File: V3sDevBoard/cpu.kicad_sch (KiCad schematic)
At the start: 1 part, among them U1 Allwinner_V3s

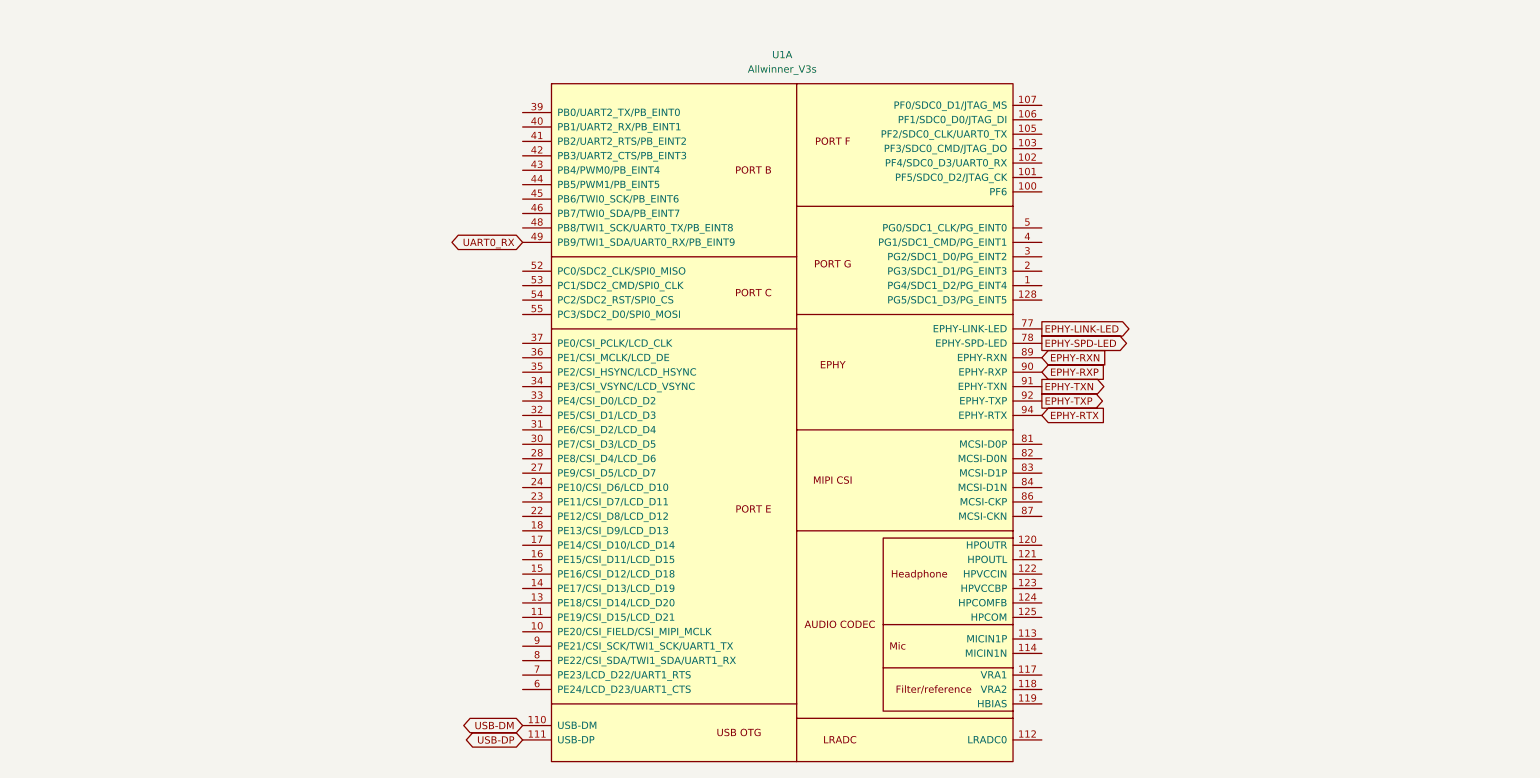
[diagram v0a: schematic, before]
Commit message: drawing schematic
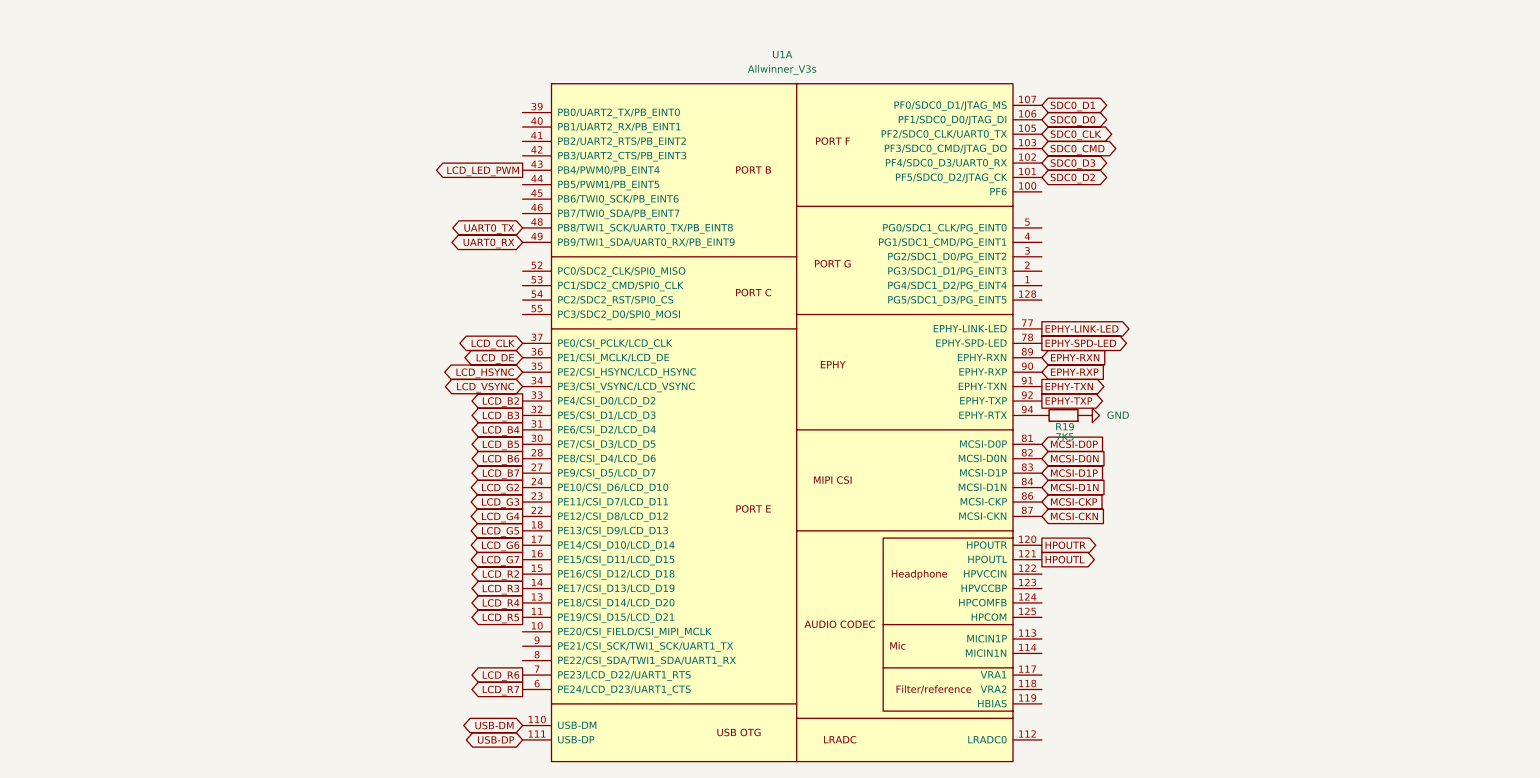
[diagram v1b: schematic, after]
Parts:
- added R19: 7K5, symbol Device:R
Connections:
- net SDC0_D2: now reaches U1.101 (PF5/SDC0_D2/JTAG_CK)
- net SDC0_D3: now reaches U1.102 (PF4/SDC0_D3/UART0_RX)
- net SDC0_CMD: now reaches U1.103 (PF3/SDC0_CMD/JTAG_DO)
- net SDC0_CLK: now reaches U1.105 (PF2/SDC0_CLK/UART0_TX)
- net SDC0_D0: now reaches U1.106 (PF1/SDC0_D0/JTAG_DI)
- net SDC0_D1: now reaches U1.107 (PF0/SDC0_D1/JTAG_MS)
- net LCD_R5: now reaches U1.11 (PE19/CSI_D15/LCD_D21)
- net HPOUTR: now reaches U1.120 (HPOUTR)
- net HPOUTL: now reaches U1.121 (HPOUTL)
- net LCD_R4: now reaches U1.13 (PE18/CSI_D14/LCD_D20)
- net LCD_R3: now reaches U1.14 (PE17/CSI_D13/LCD_D19)
- net LCD_R2: now reaches U1.15 (PE16/CSI_D12/LCD_D18)
- net LCD_G7: now reaches U1.16 (PE15/CSI_D11/LCD_D15)
- net LCD_G6: now reaches U1.17 (PE14/CSI_D10/LCD_D14)
- net LCD_G5: now reaches U1.18 (PE13/CSI_D9/LCD_D13)
- net LCD_G4: now reaches U1.22 (PE12/CSI_D8/LCD_D12)
- net LCD_G3: now reaches U1.23 (PE11/CSI_D7/LCD_D11)
- net LCD_G2: now reaches U1.24 (PE10/CSI_D6/LCD_D10)
- net LCD_B7: now reaches U1.27 (PE9/CSI_D5/LCD_D7)
- net LCD_B6: now reaches U1.28 (PE8/CSI_D4/LCD_D6)
- net LCD_B5: now reaches U1.30 (PE7/CSI_D3/LCD_D5)
- net LCD_B4: now reaches U1.31 (PE6/CSI_D2/LCD_D4)
- net LCD_B3: now reaches U1.32 (PE5/CSI_D1/LCD_D3)
- net LCD_B2: now reaches U1.33 (PE4/CSI_D0/LCD_D2)
- net LCD_VSYNC: now reaches U1.34 (PE3/CSI_VSYNC/LCD_VSYNC)
- net LCD_HSYNC: now reaches U1.35 (PE2/CSI_HSYNC/LCD_HSYNC)
- net LCD_DE: now reaches U1.36 (PE1/CSI_MCLK/LCD_DE)
- net LCD_CLK: now reaches U1.37 (PE0/CSI_PCLK/LCD_CLK)
- net LCD_LED_PWM: now reaches U1.43 (PB4/PWM0/PB_EINT4)
- net UART0_TX: now reaches U1.48 (PB8/TWI1_SCK/UART0_TX/PB_EINT8)
- net LCD_R7: now reaches U1.6 (PE24/LCD_D23/UART1_CTS)
- net LCD_R6: now reaches U1.7 (PE23/LCD_D22/UART1_RTS)
- net MCSI-D0P: now reaches U1.81 (MCSI-D0P)
- net MCSI-D0N: now reaches U1.82 (MCSI-D0N)
- net MCSI-D1P: now reaches U1.83 (MCSI-D1P)
- net MCSI-D1N: now reaches U1.84 (MCSI-D1N)
- net MCSI-CKP: now reaches U1.86 (MCSI-CKP)
- net MCSI-CKN: now reaches U1.87 (MCSI-CKN)
- net EPHY-RTX: no longer names the net of U1.94 (EPHY-RTX)
- net EPHY-RTX: now also R19.1
- new net GND: R19.2

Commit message: drawing schematics
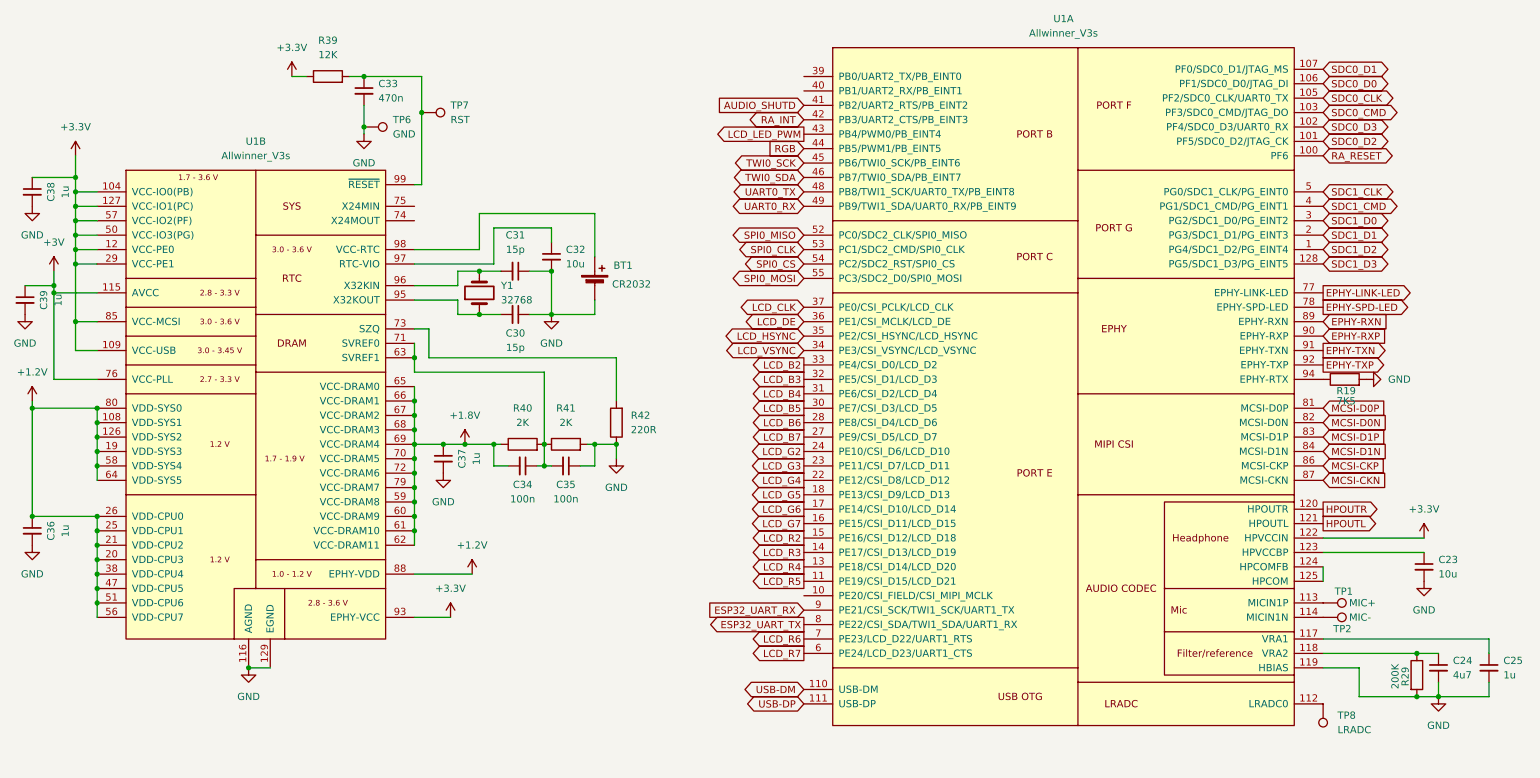
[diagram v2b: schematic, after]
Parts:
- added BT1: CR2032, Battery:BatteryHolder_MYOUNG_BS-07-A1BJ001_CR2032, symbol Device:Battery_Cell
- added C23, C32: 10u, Capacitor_SMD:C_0805_2012Metric_Pad1.18x1.45mm_HandSolder, symbol Device:C_Small
- added C24: 4u7, Capacitor_SMD:C_0805_2012Metric_Pad1.18x1.45mm_HandSolder, symbol Device:C_Small
- added C25, C36, C37, C38, C39: 1u, Capacitor_SMD:C_0805_2012Metric_Pad1.18x1.45mm_HandSolder, symbol Device:C_Small
- added C30, C31: 15p, Capacitor_SMD:C_0805_2012Metric_Pad1.18x1.45mm_HandSolder, symbol Device:C_Small
- added C33: 470n, Capacitor_SMD:C_0805_2012Metric_Pad1.18x1.45mm_HandSolder, symbol Device:C_Small
- added C34, C35: 100n, Capacitor_SMD:C_0805_2012Metric_Pad1.18x1.45mm_HandSolder, symbol Device:C_Small
- added R29: 200K, Resistor_SMD:R_0805_2012Metric_Pad1.20x1.40mm_HandSolder, symbol Device:R
- added R39: 12K, Resistor_SMD:R_0805_2012Metric_Pad1.20x1.40mm_HandSolder, symbol Device:R
- added R40, R41: 2K, Resistor_SMD:R_0805_2012Metric_Pad1.20x1.40mm_HandSolder, symbol Device:R
- added R42: 220R, Resistor_SMD:R_0805_2012Metric_Pad1.20x1.40mm_HandSolder, symbol Device:R
- added TP1: MIC+, TestPoint:TestPoint_Pad_D1.0mm, symbol Connector:TestPoint
- added TP2: MIC-, TestPoint:TestPoint_Pad_D1.0mm, symbol Connector:TestPoint
- added TP6: GND, TestPoint:TestPoint_Pad_D1.5mm, symbol Connector:TestPoint
- added TP7: RST, TestPoint:TestPoint_Pad_D1.5mm, symbol Connector:TestPoint
- added TP8: LRADC, TestPoint:TestPoint_Pad_D1.0mm, symbol Connector:TestPoint
- added unit 1 of U1
- added Y1: 32768, Crystal:Crystal_SMD_Abracon_ABS25-4Pin_8.0x3.8mm, symbol Device:Crystal
- R19: footprint (none) -> Resistor_SMD:R_0805_2012Metric_Pad1.20x1.40mm_HandSolder
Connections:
- net EPHY-LINK-LED: now also U1.77 (EPHY-LINK-LED); no longer U1.77 (EPHY-LINK-LED)
- net EPHY-RXN: now also U1.89 (EPHY-RXN); no longer U1.89 (EPHY-RXN)
- net EPHY-RXP: now also U1.90 (EPHY-RXP); no longer U1.90 (EPHY-RXP)
- net EPHY-SPD-LED: now also U1.78 (EPHY-SPD-LED); no longer U1.78 (EPHY-SPD-LED)
- net EPHY-TXN: now also U1.91 (EPHY-TXN); no longer U1.91 (EPHY-TXN)
- net EPHY-TXP: now also U1.92 (EPHY-TXP); no longer U1.92 (EPHY-TXP)
- net GND: now also U1.116 (AGND), U1.129 (EGND), BT1.2 (-), C23.2, C24.2, C25.2, C30.1, C31.1, C32.2, C33.2, C35.1, C36.2, C37.2, C38.2, C39.2, R29.2, R41.2, R42.1, TP6.1, U1.119 (HBIAS)
- net HPOUTL: now also U1.121 (HPOUTL); no longer U1.121 (HPOUTL)
- net HPOUTR: now also U1.120 (HPOUTR); no longer U1.120 (HPOUTR)
- net LCD_B2: now also U1.33 (PE4/CSI_D0/LCD_D2); no longer U1.33 (PE4/CSI_D0/LCD_D2)
- net LCD_B3: now also U1.32 (PE5/CSI_D1/LCD_D3); no longer U1.32 (PE5/CSI_D1/LCD_D3)
- net LCD_B4: now also U1.31 (PE6/CSI_D2/LCD_D4); no longer U1.31 (PE6/CSI_D2/LCD_D4)
- net LCD_B5: now also U1.30 (PE7/CSI_D3/LCD_D5); no longer U1.30 (PE7/CSI_D3/LCD_D5)
- net LCD_B6: now also U1.28 (PE8/CSI_D4/LCD_D6); no longer U1.28 (PE8/CSI_D4/LCD_D6)
- net LCD_B7: now also U1.27 (PE9/CSI_D5/LCD_D7); no longer U1.27 (PE9/CSI_D5/LCD_D7)
- net LCD_CLK: now also U1.37 (PE0/CSI_PCLK/LCD_CLK); no longer U1.37 (PE0/CSI_PCLK/LCD_CLK)
- net LCD_DE: now also U1.36 (PE1/CSI_MCLK/LCD_DE); no longer U1.36 (PE1/CSI_MCLK/LCD_DE)
- net LCD_G2: now also U1.24 (PE10/CSI_D6/LCD_D10); no longer U1.24 (PE10/CSI_D6/LCD_D10)
- net LCD_G3: now also U1.23 (PE11/CSI_D7/LCD_D11); no longer U1.23 (PE11/CSI_D7/LCD_D11)
- net LCD_G4: now also U1.22 (PE12/CSI_D8/LCD_D12); no longer U1.22 (PE12/CSI_D8/LCD_D12)
- net LCD_G5: now also U1.18 (PE13/CSI_D9/LCD_D13); no longer U1.18 (PE13/CSI_D9/LCD_D13)
- net LCD_G6: now also U1.17 (PE14/CSI_D10/LCD_D14); no longer U1.17 (PE14/CSI_D10/LCD_D14)
- net LCD_G7: now also U1.16 (PE15/CSI_D11/LCD_D15); no longer U1.16 (PE15/CSI_D11/LCD_D15)
- net LCD_HSYNC: now also U1.35 (PE2/CSI_HSYNC/LCD_HSYNC); no longer U1.35 (PE2/CSI_HSYNC/LCD_HSYNC)
- net LCD_LED_PWM: now also U1.43 (PB4/PWM0/PB_EINT4); no longer U1.43 (PB4/PWM0/PB_EINT4)
- net LCD_R2: now also U1.15 (PE16/CSI_D12/LCD_D18); no longer U1.15 (PE16/CSI_D12/LCD_D18)
- net LCD_R3: now also U1.14 (PE17/CSI_D13/LCD_D19); no longer U1.14 (PE17/CSI_D13/LCD_D19)
- net LCD_R4: now also U1.13 (PE18/CSI_D14/LCD_D20); no longer U1.13 (PE18/CSI_D14/LCD_D20)
- net LCD_R5: now also U1.11 (PE19/CSI_D15/LCD_D21); no longer U1.11 (PE19/CSI_D15/LCD_D21)
- net LCD_R6: now also U1.7 (PE23/LCD_D22/UART1_RTS); no longer U1.7 (PE23/LCD_D22/UART1_RTS)
- net LCD_R7: now also U1.6 (PE24/LCD_D23/UART1_CTS); no longer U1.6 (PE24/LCD_D23/UART1_CTS)
- net LCD_VSYNC: now also U1.34 (PE3/CSI_VSYNC/LCD_VSYNC); no longer U1.34 (PE3/CSI_VSYNC/LCD_VSYNC)
- net MCSI-CKN: now also U1.87 (MCSI-CKN); no longer U1.87 (MCSI-CKN)
- net MCSI-CKP: now also U1.86 (MCSI-CKP); no longer U1.86 (MCSI-CKP)
- net MCSI-D0N: now also U1.82 (MCSI-D0N); no longer U1.82 (MCSI-D0N)
- net MCSI-D0P: now also U1.81 (MCSI-D0P); no longer U1.81 (MCSI-D0P)
- net MCSI-D1N: now also U1.84 (MCSI-D1N); no longer U1.84 (MCSI-D1N)
- net MCSI-D1P: now also U1.83 (MCSI-D1P); no longer U1.83 (MCSI-D1P)
- net SDC0_CLK: now also U1.105 (PF2/SDC0_CLK/UART0_TX); no longer U1.105 (PF2/SDC0_CLK/UART0_TX)
- net SDC0_CMD: now also U1.103 (PF3/SDC0_CMD/JTAG_DO); no longer U1.103 (PF3/SDC0_CMD/JTAG_DO)
- net SDC0_D0: now also U1.106 (PF1/SDC0_D0/JTAG_DI); no longer U1.106 (PF1/SDC0_D0/JTAG_DI)
- net SDC0_D1: now also U1.107 (PF0/SDC0_D1/JTAG_MS); no longer U1.107 (PF0/SDC0_D1/JTAG_MS)
- net SDC0_D2: now also U1.101 (PF5/SDC0_D2/JTAG_CK); no longer U1.101 (PF5/SDC0_D2/JTAG_CK)
- net SDC0_D3: now also U1.102 (PF4/SDC0_D3/UART0_RX); no longer U1.102 (PF4/SDC0_D3/UART0_RX)
- net UART0_RX: now also U1.49 (PB9/TWI1_SDA/UART0_RX/PB_EINT9); no longer U1.49 (PB9/TWI1_SDA/UART0_RX/PB_EINT9)
- net UART0_TX: now also U1.48 (PB8/TWI1_SCK/UART0_TX/PB_EINT8); no longer U1.48 (PB8/TWI1_SCK/UART0_TX/PB_EINT8)
- net USB-DM: now also U1.110 (USB-DM); no longer U1.110 (USB-DM)
- net USB-DP: now also U1.111 (USB-DP); no longer U1.111 (USB-DP)
- net at R19.1: now also U1.94 (EPHY-RTX); no longer U1.94 (EPHY-RTX)
- new net: TP1.1, U1.113 (MICIN1P)
- new net: TP2.1, U1.114 (MICIN1N)
- new net: C34.1, C35.2, R40.2, R41.1, U1.63 (SVREF1), U1.71 (SVREF0)
- new net: R42.2, U1.73 (SZQ)
- new net: C30.2, U1.95 (X32KOUT), Y1.1
- new net: C31.2, U1.96 (X32KIN), Y1.4 (2)
- new net: C32.1, U1.97 (RTC-VIO)
- new net: BT1.1 (+), U1.98 (VCC-RTC)
- new net: C33.1, R39.2, TP7.1, U1.99 (~{RESET})
- new net: TP8.1, U1.112 (LRADC0)
- new net: C25.1, U1.117 (VRA1)
- new net: C24.1, R29.1, U1.118 (VRA2)
- new net: C23.1, U1.123 (HPVCCBP)
- new net: U1.124 (HPCOMFB), U1.125 (HPCOM)
- new net +1.2V: C36.1, U1.108 (VDD-SYS1), U1.126 (VDD-SYS2), U1.19 (VDD-SYS3), U1.20 (VDD-CPU3), U1.21 (VDD-CPU2), U1.25 (VDD-CPU1), U1.26 (VDD-CPU0), U1.38 (VDD-CPU4), U1.47 (VDD-CPU5), U1.51 (VDD-CPU6), U1.56 (VDD-CPU7), U1.58 (VDD-SYS4), U1.64 (VDD-SYS5), U1.80 (VDD-SYS0), U1.88 (EPHY-VDD)
- new net +1.8V: C34.2, C37.1, R40.1, U1.59 (VCC-DRAM8), U1.60 (VCC-DRAM9), U1.61 (VCC-DRAM10), U1.62 (VCC-DRAM11), U1.65 (VCC-DRAM0), U1.66 (VCC-DRAM1), U1.67 (VCC-DRAM2), U1.68 (VCC-DRAM3), U1.69 (VCC-DRAM4), U1.70 (VCC-DRAM5), U1.72 (VCC-DRAM6), U1.79 (VCC-DRAM7)
- new net +3.3V: C38.1, R39.1, U1.104 (VCC-IO0(PB)), U1.109 (VCC-USB), U1.12 (VCC-PE0), U1.122 (HPVCCIN), U1.127 (VCC-IO1(PC)), U1.29 (VCC-PE1), U1.50 (VCC-IO3(PG)), U1.57 (VCC-IO2(PF)), U1.85 (VCC-MCSI), U1.93 (EPHY-VCC)
- new net +3V: C39.1, U1.115 (AVCC), U1.76 (VCC-PLL)
- new net AUDIO_SHUTD: U1.41 (PB2/UART2_RTS/PB_EINT2)
- new net ESP32_UART_RX: U1.9 (PE21/CSI_SCK/TWI1_SCK/UART1_TX)
- new net ESP32_UART_TX: U1.8 (PE22/CSI_SDA/TWI1_SDA/UART1_RX)
- new net RA_INT: U1.42 (PB3/UART2_CTS/PB_EINT3)
- new net RA_RESET: U1.100 (PF6)
- new net RGB: U1.44 (PB5/PWM1/PB_EINT5)
- new net SDC1_CLK: U1.5 (PG0/SDC1_CLK/PG_EINT0)
- new net SDC1_CMD: U1.4 (PG1/SDC1_CMD/PG_EINT1)
- new net SDC1_D0: U1.3 (PG2/SDC1_D0/PG_EINT2)
- new net SDC1_D1: U1.2 (PG3/SDC1_D1/PG_EINT3)
- new net SDC1_D2: U1.1 (PG4/SDC1_D2/PG_EINT4)
- new net SDC1_D3: U1.128 (PG5/SDC1_D3/PG_EINT5)
- new net SPI0_CLK: U1.53 (PC1/SDC2_CMD/SPI0_CLK)
- new net SPI0_CS: U1.54 (PC2/SDC2_RST/SPI0_CS)
- new net SPI0_MISO: U1.52 (PC0/SDC2_CLK/SPI0_MISO)
- new net SPI0_MOSI: U1.55 (PC3/SDC2_D0/SPI0_MOSI)
- new net TWI0_SCK: U1.45 (PB6/TWI0_SCK/PB_EINT6)
- new net TWI0_SDA: U1.46 (PB7/TWI0_SDA/PB_EINT7)
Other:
- company: (none) -> J.K.
- title: (none) -> V3s Dev Board
- moved on the sheet: R19

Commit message: advancing in schematics and footprints
Making needed custom footprints for connectors, adding a lot of small changes to schematics.
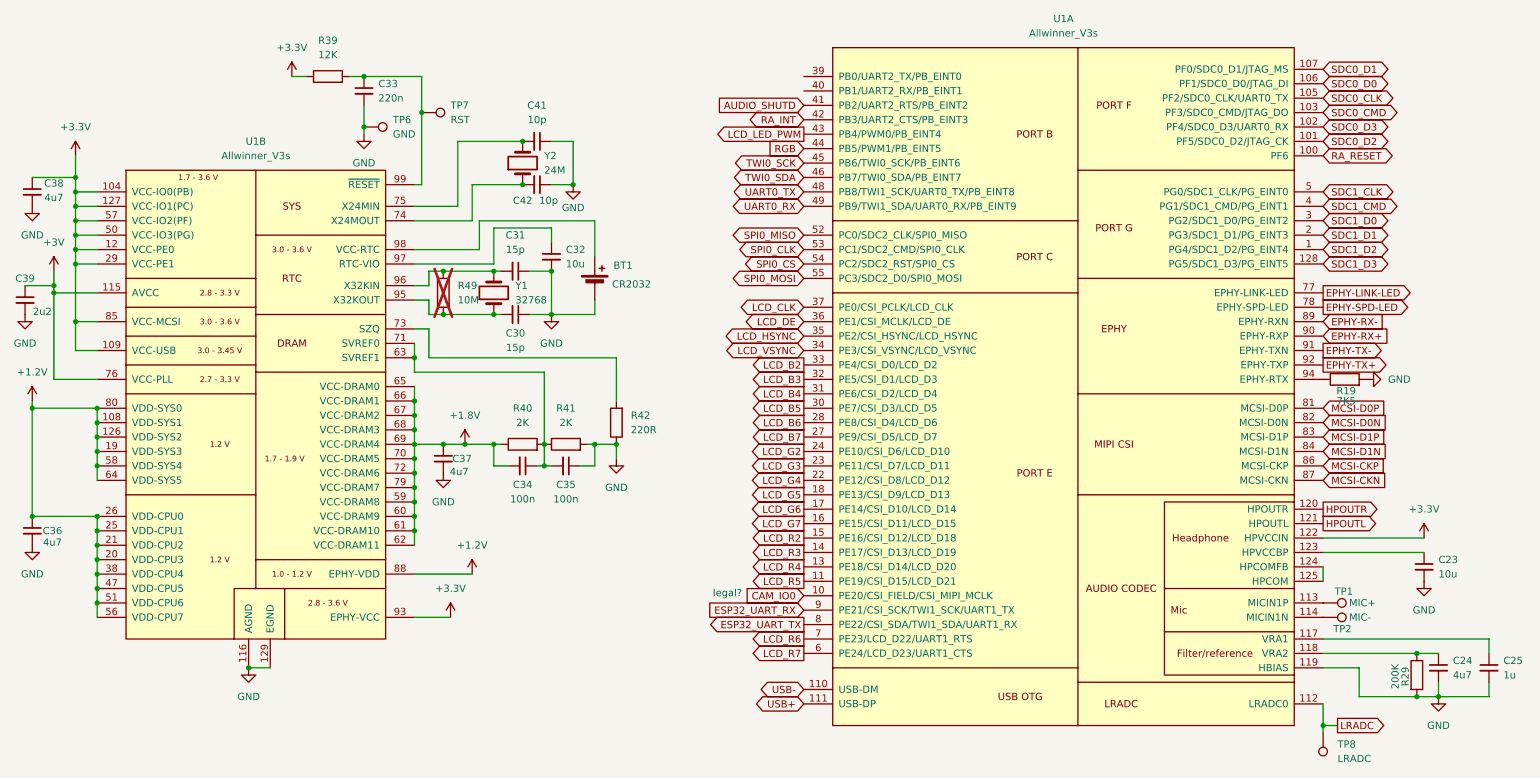
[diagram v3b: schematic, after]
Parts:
- added C41, C42: 10p, Capacitor_SMD:C_0805_2012Metric_Pad1.18x1.45mm_HandSolder, symbol Device:C_Small
- added R49: 10M, Resistor_SMD:R_0805_2012Metric_Pad1.20x1.40mm_HandSolder, symbol Device:R
- added Y2: 24M, Crystal:Crystal_HC49-4H_Vertical, symbol Device:Crystal
- C33: value 470n -> 220n
- C36, C37, C38: value 1u -> 4u7
- C39: value 1u -> 2u2
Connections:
- net GND: now also C41.1, C42.1
- net at U1.74 (X24MOUT): now also C42.2, Y2.1
- net at U1.75 (X24MIN): now also C41.2, Y2.4 (2)
- net at C30.2, U1.95 (X32KOUT), Y1.1: now also R49.1
- net at C31.2, U1.96 (X32KIN), Y1.4 (2): now also R49.2
- net CAM_IO0: now reaches U1.10 (PE20/CSI_FIELD/CSI_MIPI_MCLK)
- net LRADC: now reaches TP8.1, U1.112 (LRADC0)
- net EPHY-RXN renamed EPHY-RX-
- net EPHY-RXP renamed EPHY-RX+
- net EPHY-TXN renamed EPHY-TX-
- net EPHY-TXP renamed EPHY-TX+
- net USB-DM renamed USB-
- net USB-DP renamed USB+
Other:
- note added: "legal?"
- title: V3s Dev Board -> V3s_Dev_Board
- moved on the sheet: TP8, Y1

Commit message: completing schematics
completing schematics, adding netclasses, fixing bugs, updating readme, starting pcb
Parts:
- added R63, R64, R65, R66: 33R, Resistor_SMD:R_0603_1608Metric_Pad0.98x0.95mm_HandSolder, symbol Device:R
- added R67: 470R, Resistor_SMD:R_0603_1608Metric_Pad0.98x0.95mm_HandSolder, symbol Device:R
- added TP18: CAM_IO0, TestPoint:TestPoint_Pad_D1.0mm, symbol Connector:TestPoint
- added TP19: PF6, TestPoint:TestPoint_Pad_D1.0mm, symbol Connector:TestPoint
- C32: value 10u -> 4u7
- R19: value 7K5 -> 5K6; footprint Resistor_SMD:R_0805_2012Metric_Pad1.20x1.40mm_HandSolder -> Resistor_SMD:R_0603_1608Metric_Pad0.98x0.95mm_HandSolder
- R42: value 220R -> 240R 1%
- TP1, TP2: footprint TestPoint:TestPoint_Pad_D1.0mm -> TestPoint:TestPoint_Pad_1.0x1.0mm
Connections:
- net AUDIO_SHUTD is gone; now on net RA_RESET: U1.41 (PB2/UART2_RTS/PB_EINT2)
- net CAM_IO0: now also TP18.1
- net ESP32_UART_RX: now also U1.39 (PB0/UART2_TX/PB_EINT0); no longer U1.9 (PE21/CSI_SCK/TWI1_SCK/UART1_TX)
- net ESP32_UART_TX: now also U1.40 (PB1/UART2_RX/PB_EINT1); no longer U1.8 (PE22/CSI_SDA/TWI1_SDA/UART1_RX)
- net GND: now also R67.2; no longer R19.2
- net LCD_CLK: now also R64.1; no longer U1.37 (PE0/CSI_PCLK/LCD_CLK)
- net RA_RESET: no longer U1.100 (PF6)
- net SDC0_CLK: now also R63.2; no longer U1.105 (PF2/SDC0_CLK/UART0_TX)
- net SDC1_CLK: now also R66.2; no longer U1.5 (PG0/SDC1_CLK/PG_EINT0)
- net SPI0_CLK: now also R65.1; no longer U1.53 (PC1/SDC2_CMD/SPI0_CLK)
- net at C41.2, U1.75 (X24MIN): now also Y2.2; no longer Y2.4 (2)
- net HPCOM: now reaches U1.124 (HPCOMFB), U1.125 (HPCOM)
- new net: R64.2, U1.37 (PE0/CSI_PCLK/LCD_CLK)
- new net: R63.1, U1.105 (PF2/SDC0_CLK/UART0_TX)
- new net: R66.1, U1.5 (PG0/SDC1_CLK/PG_EINT0)
- new net: R65.2, U1.53 (PC1/SDC2_CMD/SPI0_CLK)
- new net: R19.2, R67.1
- new net CSI_SCK: U1.9 (PE21/CSI_SCK/TWI1_SCK/UART1_TX)
- new net CSI_SDA: U1.8 (PE22/CSI_SDA/TWI1_SDA/UART1_RX)
- new net PF6: TP19.1, U1.100 (PF6)
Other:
- note removed: "legal?"
- company: J.K. -> jakub.kmiecik@protonmail.com
